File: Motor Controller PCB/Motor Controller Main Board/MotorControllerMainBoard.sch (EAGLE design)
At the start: 99 parts, among them T1 TEENSY_3.1_ALL_PINS

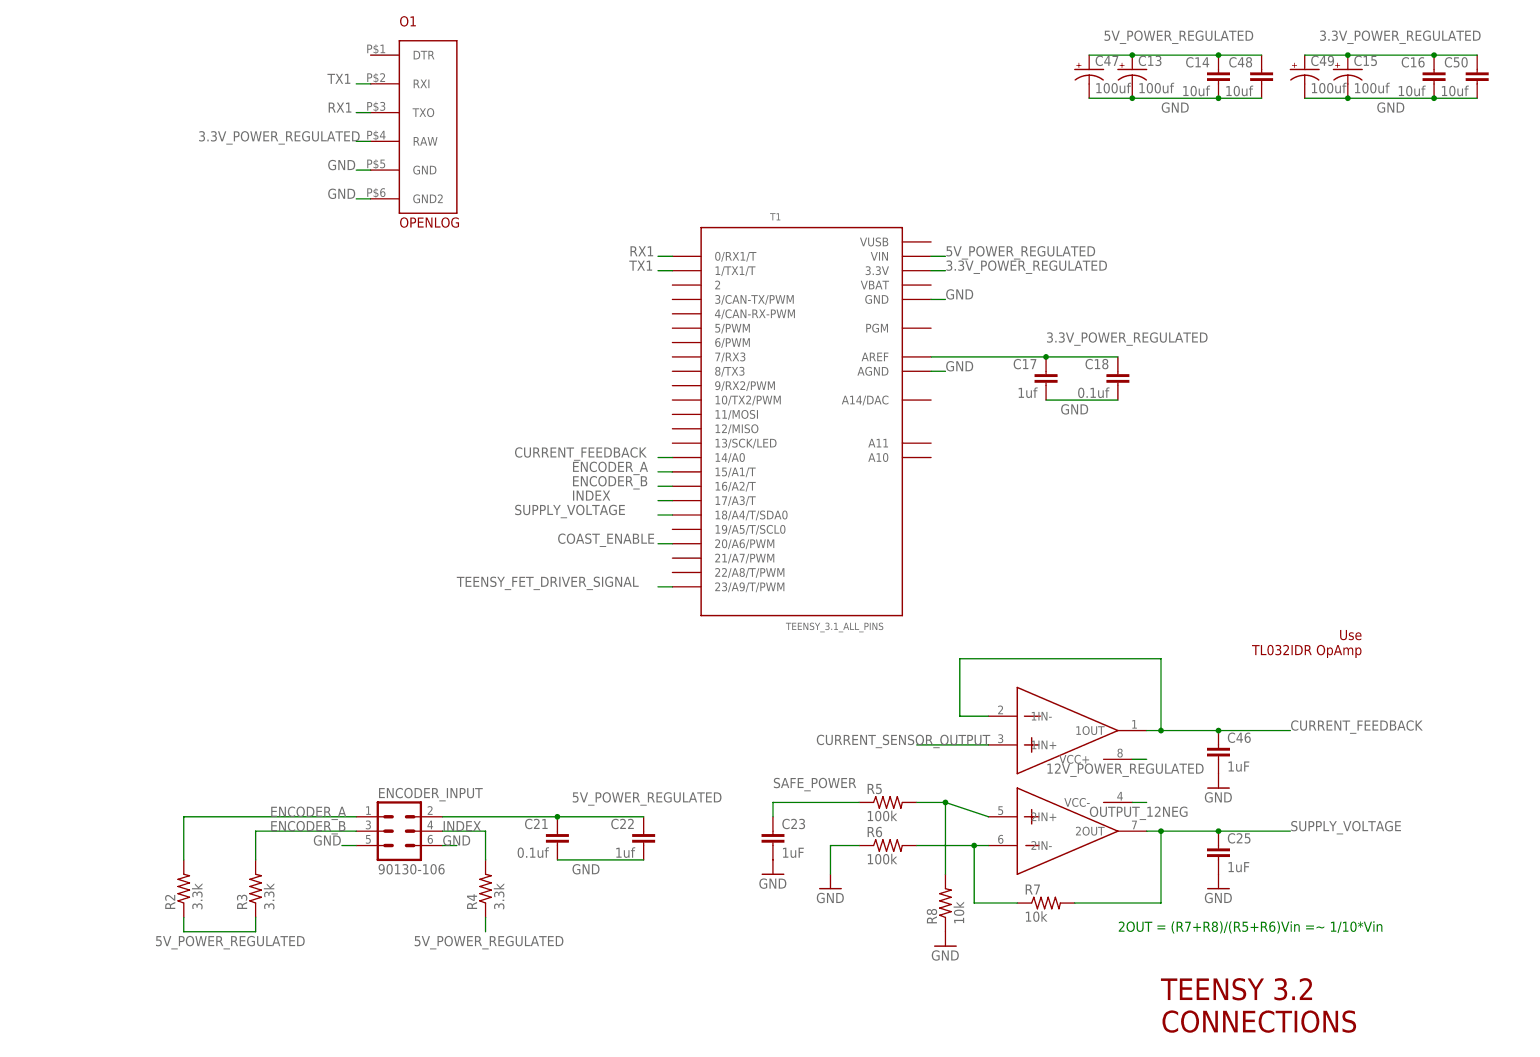
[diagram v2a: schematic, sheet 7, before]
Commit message: Board work and removed some caps
-Removed 2 caps from 5V reg and 12V and -12V reg
-Removed 5 caps from input filter and 5 ceramics
-Larger components are in place, I started wiring the input caps.
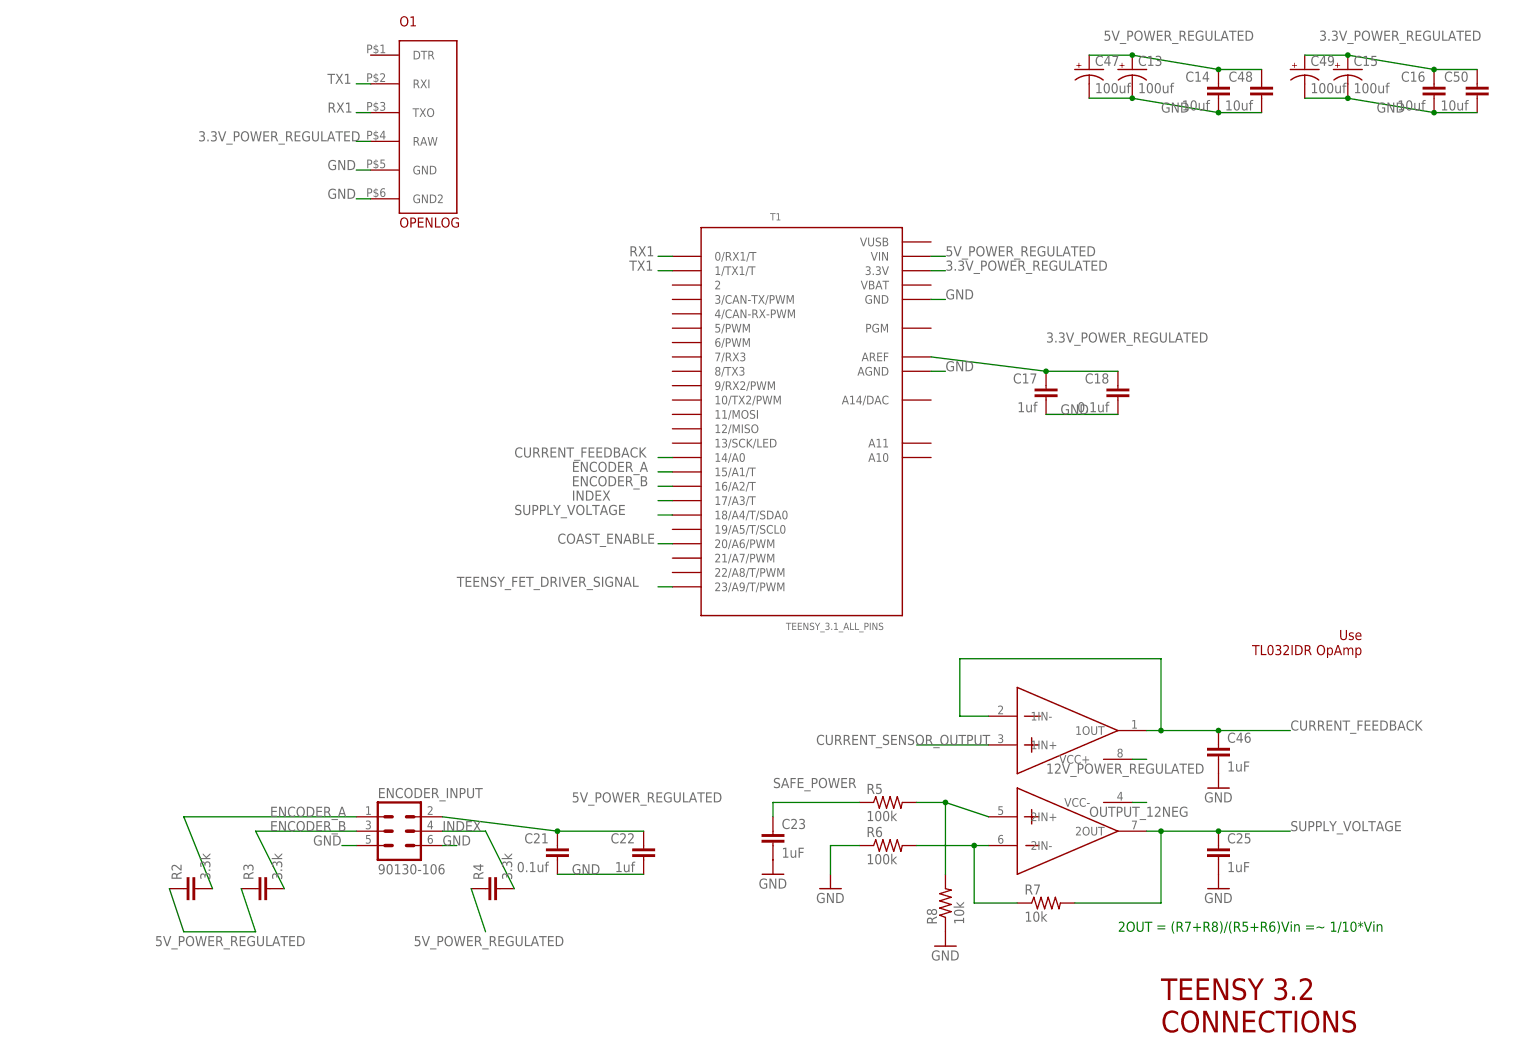
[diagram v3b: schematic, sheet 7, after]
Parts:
- removed C11, C12, C7, C8: EEUFR1H221B, MotorControllerEagleLibrary:EEUFR1H221B
- removed C31, C32, C33, C34, C35: EEU-FR1H331L, MotorControllerEagleLibrary:EEU-FR1H331L
- removed C41, C42, C43, C44, C45: (no value), resistor:C-EUC1206
- removed C54: 10uF, resistor:C-EUC0805
- removed C58: (no value), resistor:C-EUC0805
- C14, C16, C17, C18, C19, C20, C21, C22, C26, C48, C50: device SparkFun-Capacitors:CAP0805 -> resistor:C-EUC0805
- R2, R3, R4: device SparkFun-Passives:RESISTOR0805-RES -> resistor:C-EUC0805
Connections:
- net 12V_POWER_REGULATED: no longer C7.11, C8.11
- net 5V_POWER_REGULATED: no longer C11.11, C12.11
- net GND: no longer C11.22, C12.22, C31.22, C32.22, C33.22, C34.22, C35.22, C41.2, C42.2, C43.2, C44.2, C45.2, C58.2, C7.22, C8.22
- net MAIN_POWER_IN(+): no longer C31.11, C32.11, C33.11, C34.11, C35.11, C41.1, C42.1, C43.1, C44.1, C45.1
- net N$14: no longer C54.1
- net N$15: no longer C54.2
- net OUTPUT_12NEG: no longer C58.1
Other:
- note added: "330uF Electro. Caps 1.65mF in total Low ESL, Low ESR"
- note added: "GRM31CR61H106KA12K Ceramic Capacitor 10uF each 50uF in total Very low ESL, Very low ESR"
- note removed: "330uF Electro. Caps 3.3mF in total Low ESL, Low ESR"
- note removed: "GRM31CR61H106KA12K Ceramic Capacitor 10uF each 100uF in total Very low ESL, Very low ESR"
- moved on the sheet: C14, C16, C17, C18, C19, C20, C21, C22, C26, C48, C50

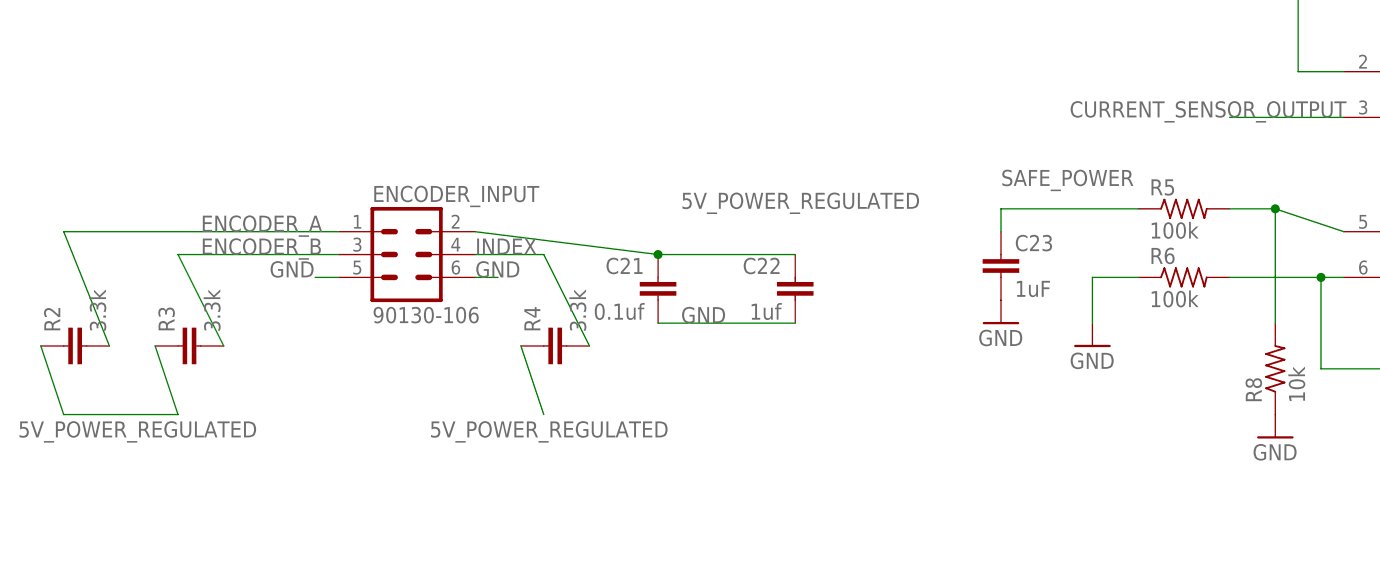
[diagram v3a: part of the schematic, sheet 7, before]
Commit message: Placed all components on board
-They just need wiring.
-Yes I know it looks sloppy, but we need a quick prototype.
-Final version of the board will have more thought into component
placement
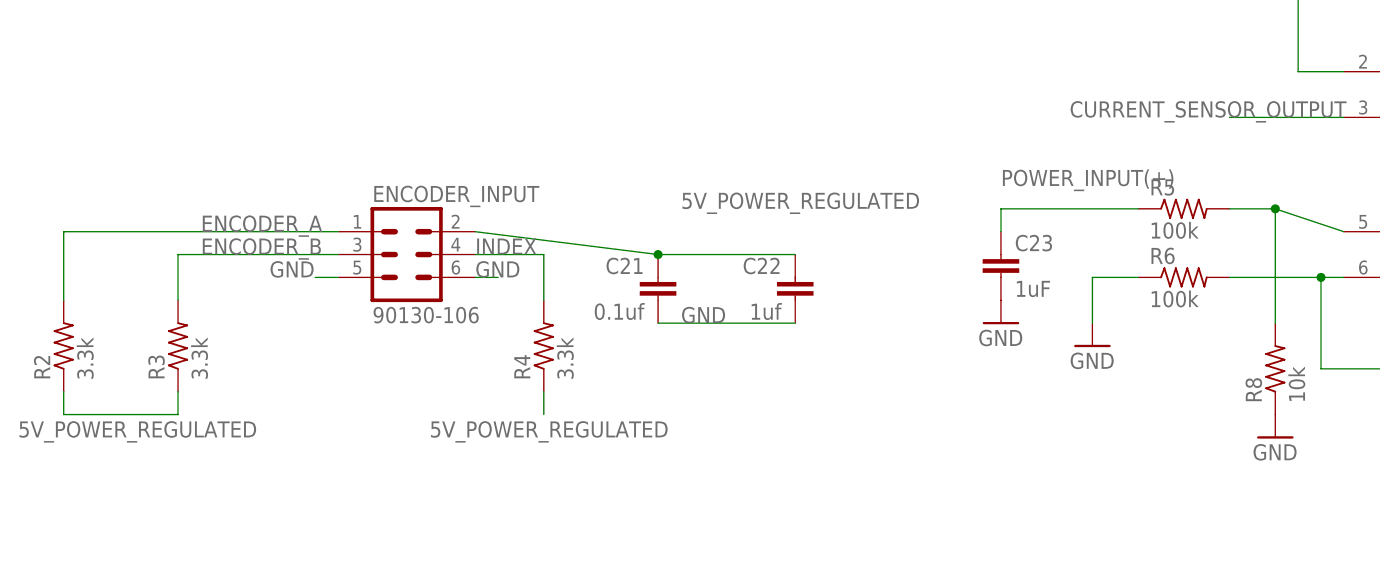
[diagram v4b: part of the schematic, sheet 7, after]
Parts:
- R2, R3, R4: device resistor:C-EUC0805 -> resistor:R-US_R0805
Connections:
- net MAIN_POWER_IN(+) renamed INPUT_POWER(+)
- net SAFE_POWER renamed POWER_INPUT(+)
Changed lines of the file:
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@@
 <part name="C21" library="resistor" library_urn="urn:adsk.eagle:library:348" deviceset="C-EU" device="C0805" package3d_urn="urn:adsk.eagle:package:26137/1" value="0.1uf"/>
 <part name="C22" library="resistor" library_urn="urn:adsk.eagle:library:348" deviceset="C-EU" device="C0805" package3d_urn="urn:adsk.eagle:package:26137/1" value="1uf"/>
-<part name="R2" library="resistor" library_urn="urn:adsk.eagle:library:348" deviceset="C-EU" device="C0805" package3d_urn="urn:adsk.eagle:package:26137/1" value="3.3k"/>
-<part name="R3" library="resistor" library_urn="urn:adsk.eagle:library:348" deviceset="C-EU" device="C0805" package3d_urn="urn:adsk.eagle:package:26137/1" value="3.3k"/>
-<part name="R4" library="resistor" library_urn="urn:adsk.eagle:library:348" deviceset="C-EU" device="C0805" package3d_urn="urn:adsk.eagle:package:26137/1" value="3.3k"/>
+<part name="R2" library="resistor" library_urn="urn:adsk.eagle:library:348" deviceset="R-US_" device="R0805" package3d_urn="urn:adsk.eagle:package:26059/1" value="3.3k"/>
+<part name="R3" library="resistor" library_urn="urn:adsk.eagle:library:348" deviceset="R-US_" device="R0805" package3d_urn="urn:adsk.eagle:package:26059/1" value="3.3k"/>
+<part name="R4" library="resistor" library_urn="urn:adsk.eagle:library:348" deviceset="R-US_" device="R0805" package3d_urn="urn:adsk.eagle:package:26059/1" value="3.3k"/>
 <part name="L1" library="SparkFun (2015_10_14 22_27_04 UTC)" deviceset="INDUCTOR" device="0805" value="42nH"/>
 <part name="AD8512ARZ" library="MotorControllerEagleLibrary" deviceset="TL072CDT" device=""/>
@@
 </busses>
 <nets>
-<net name="SAFE_POWER" class="0">
-<segment>
-<wire x1="78.74" y1="182.88" x2="109.22" y2="182.88" width="0.1524" layer="91"/>
-<label x="86.36" y="185.42" size="1.778" layer="95"/>
-</segment>
-</net>
 <net name="MOTOR_OUTPUT_(--)" class="0">
 <segment>
@@
 </segment>
 </net>
-<net name="MAIN_POWER_IN(+)" class="0">
+<net name="INPUT_POWER(+)" class="0">
 <segment>
 <label x="22.86" y="170.18" size="1.778" layer="95" rot="R270"/>
 <wire x1="15.24" y1="182.88" x2="25.4" y2="182.88" width="0.1524" layer="91"/>
 <label x="12.7" y="185.42" size="1.778" layer="95"/>
-<wire x1="25.4" y1="182.88" x2="55.88" y2="182.88" width="0.1524" layer="91"/>
+<wire x1="25.4" y1="182.88" x2="48.26" y2="182.88" width="0.1524" layer="91"/>
 <junction x="25.4" y="182.88"/>
+<wire x1="48.26" y1="182.88" x2="55.88" y2="182.88" width="0.1524" layer="91"/>
 <wire x1="25.4" y1="142.24" x2="25.4" y2="182.88" width="0.1524" layer="91"/>
 <pinref part="U$5" gate="G$1" pin="CATHODE"/>
 <pinref part="U$12" gate="G$1" pin="P$1"/>
+<wire x1="48.26" y1="182.88" x2="48.26" y2="175.26" width="0.1524" layer="91"/>
+<junction x="48.26" y="182.88"/>
+<wire x1="48.26" y1="175.26" x2="93.98" y2="175.26" width="0.1524" layer="91"/>
+<wire x1="78.74" y1="182.88" x2="93.98" y2="182.88" width="0.1524" layer="91"/>
+<label x="86.36" y="185.42" size="1.778" layer="95"/>
+<wire x1="93.98" y1="182.88" x2="109.22" y2="182.88" width="0.1524" layer="91"/>
+<wire x1="93.98" y1="175.26" x2="93.98" y2="182.88" width="0.1524" layer="91"/>
+<junction x="93.98" y="182.88"/>
 </segment>
 </net>
@@
 </segment>
 </net>
-<net name="SAFE_POWER" class="0">
+<net name="POWER_INPUT(+)" class="0">
 <segment>
 <pinref part="U$9" gate="G$1" pin="4"/>
@@
 </segment>
 </net>
-<net name="SAFE_POWER" class="0">
+<net name="POWER_INPUT(+)" class="0">
 <segment>
 <pinref part="U$6" gate="A" pin="VIN"/>
@@
 </busses>
 <nets>
-<net name="MAIN_POWER_IN(+)" class="0">
+<net name="INPUT_POWER(+)" class="0">
 <segment>
 <pinref part="C24" gate="A" pin="11"/>
@@
 <segment>
 <pinref part="R2" gate="G$1" pin="1"/>
-<wire x1="27.94" y1="50.8" x2="30.48" y2="43.18" width="0.1524" layer="91"/>
+<wire x1="30.48" y1="45.72" x2="30.48" y2="43.18" width="0.1524" layer="91"/>
 <wire x1="30.48" y1="43.18" x2="43.18" y2="43.18" width="0.1524" layer="91"/>
 <pinref part="R3" gate="G$1" pin="1"/>
-<wire x1="43.18" y1="43.18" x2="40.64" y2="50.8" width="0.1524" layer="91"/>
+<wire x1="43.18" y1="43.18" x2="43.18" y2="45.72" width="0.1524" layer="91"/>
 <label x="25.4" y="40.64" size="1.778" layer="95"/>
 </segment>
 <segment>
 <pinref part="R4" gate="G$1" pin="1"/>
-<wire x1="81.28" y1="50.8" x2="83.82" y2="43.18" width="0.1524" layer="91"/>
+<wire x1="83.82" y1="45.72" x2="83.82" y2="43.18" width="0.1524" layer="91"/>
 <label x="71.12" y="40.64" size="1.778" layer="95"/>
 </segment>
@@
 <pinref part="ENCODER_INPUT" gate="G$1" pin="1"/>
 <wire x1="60.96" y1="63.5" x2="30.48" y2="63.5" width="0.1524" layer="91"/>
-<wire x1="30.48" y1="63.5" x2="35.56" y2="50.8" width="0.1524" layer="91"/>
+<label x="45.72" y="63.5" size="1.778" layer="95"/>
 <pinref part="R2" gate="G$1" pin="2"/>
-<label x="45.72" y="63.5" size="1.778" layer="95"/>
+<wire x1="30.48" y1="55.88" x2="30.48" y2="63.5" width="0.1524" layer="91"/>
 </segment>
 </net>
@@
 <pinref part="ENCODER_INPUT" gate="G$1" pin="3"/>
 <wire x1="60.96" y1="60.96" x2="43.18" y2="60.96" width="0.1524" layer="91"/>
-<wire x1="43.18" y1="60.96" x2="48.26" y2="50.8" width="0.1524" layer="91"/>
+<wire x1="43.18" y1="60.96" x2="43.18" y2="55.88" width="0.1524" layer="91"/>
 <pinref part="R3" gate="G$1" pin="2"/>
 <label x="45.72" y="60.96" size="1.778" layer="95"/>
@@
 <pinref part="ENCODER_INPUT" gate="G$1" pin="4"/>
 <wire x1="76.2" y1="60.96" x2="83.82" y2="60.96" width="0.1524" layer="91"/>
-<wire x1="83.82" y1="60.96" x2="88.9" y2="50.8" width="0.1524" layer="91"/>
+<wire x1="83.82" y1="60.96" x2="83.82" y2="55.88" width="0.1524" layer="91"/>
 <pinref part="R4" gate="G$1" pin="2"/>
 <label x="76.2" y="60.96" size="1.778" layer="95"/>
@@
 </segment>
 </net>
-<net name="SAFE_POWER" class="0">
+<net name="POWER_INPUT(+)" class="0">
 <segment>
 <pinref part="R5" gate="G$1" pin="1"/>
